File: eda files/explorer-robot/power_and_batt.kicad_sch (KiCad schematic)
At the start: 20 parts, among them J4 Conn_01x02, Q1 Q_PMOS_GSD, U7 TPS5430DDA

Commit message: Add ADR-0021 for expansion UART and camera on PIO
Add an RGB LED connector sheet to the schematic.
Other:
- title: (none) -> Battery Power input and 5V supply
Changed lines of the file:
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@@
 	(paper "A4")
 	(title_block
+		(title "Battery Power input and 5V supply")
 		(date "2026-09-27")
 		(rev "v.0.1")

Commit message: Add LiDAR power and UART interface
Add a new lidar schematic sheet with a 4-pin connector, an
AO3400A low-side MOSFET for power switching, and gate pull
resistors. Wire LIDAR_PWR, LIDAR_TX, and LIDAR_RX hierarchical
labels into the MCU sheet and update designators.

Also shorten connector value labels to BAT, LED, and MBR.
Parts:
- J4: value Conn_01x02 -> BAT
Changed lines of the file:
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@@
 			)
 		)
-		(property "Value" "Conn_01x02"
+		(property "Value" "BAT"
 			(at 177.8 64.7699 0)
 			(show_name no)

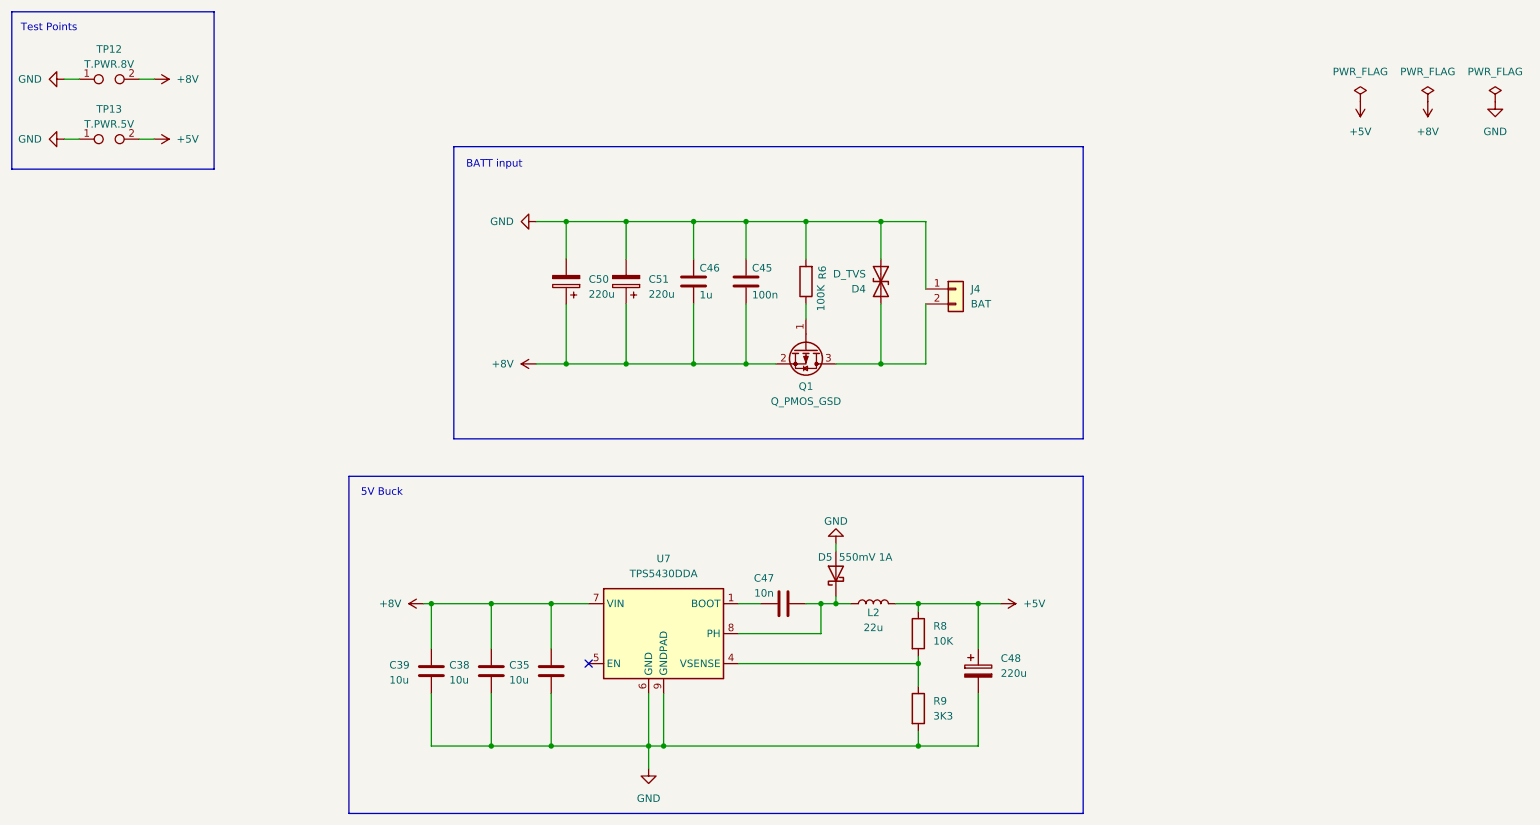
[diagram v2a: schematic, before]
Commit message: Add BATT_ADC hierarchical output to power sheet
Relocate the power/battery sheet in the schematic and expose the
battery voltage divider as a hierarchical label so it can be consumed
by the MCU.
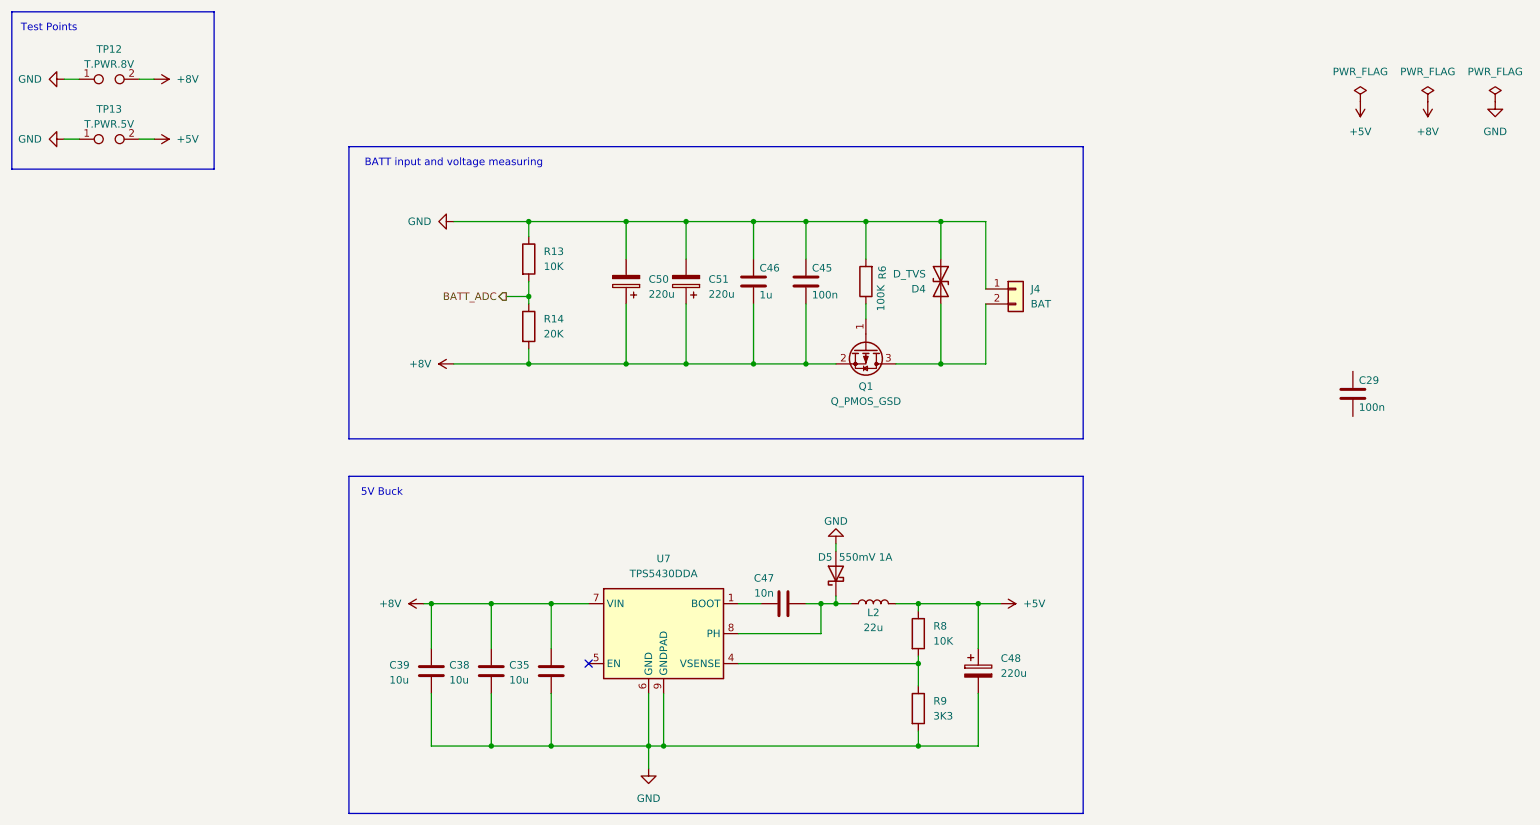
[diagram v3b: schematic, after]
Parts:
- added C29: 100n, Capacitor_SMD:C_0603_1608Metric, symbol Device:C
- added R13: 10K, Resistor_SMD:R_0603_1608Metric, symbol Device:R
- added R14: 20K, Resistor_SMD:R_0603_1608Metric, symbol Device:R
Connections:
- net +8V: now also R14.2
- net GND: now also R13.1
- new net BATT_ADC: R13.2, R14.1
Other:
- note added: "BATT input and voltage measuring"
- note removed: "BATT input"
- moved on the sheet: C45, C46, C50, C51, D4, J4, Q1, R6

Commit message: ``` Move AI camera branch to 3.3 V rail
The Grove Vision AI V2 module used here requires a 3.3 V input,
so powering it from the switched 5 V branch would over-voltage it.
Point U9 VIN at +3.3V; the TPS22917, footprint and control are
unchanged.

Also bump the 5 V inductor to 15 µH/3 A, swap the catch diode,
clean up schematic wiring and add no-connects on unused pins.
Document the decision in ADR-0025 and update ADR-0019, ADR-0021
and CONTEXT.md.
```
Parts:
- removed C29: 100n, Capacitor_SMD:C_0603_1608Metric, symbol Device:C
- D5: value 550mV 1A -> 3A 40V; JLCPCB_URL https://jlcpcb.com/partdetail/MDD_Microdiode_Semiconductor-SS14/C2480 -> https://jlcpcb.com/partdetail/MDD_Microdiode_Semiconductor-SS34/C8678; LCSC C2480 -> C8678; MPN SS14 -> SS34
- L2: value 22u -> 15u; footprint Inductor_SMD:L_APV_ANR5040 -> Inductor_SMD:L_Bourns_SRP7028A_7.3x6.6mm; JLCPCB_URL https://jlcpcb.com/partdetail/SHOUHAN-CYN504022UH/C2879700 -> https://jlcpcb.com/partdetail/SunltechTech-SLO0630H150MTT/C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; LCSC C2879700 -> C182182; MFR SHOU HAN -> Sunltech Tech; MPN CYN5040-22UH -> SLO0630H150MTT
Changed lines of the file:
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@@
 			)
 		)
-		(property "Value" "22u"
+		(property "Value" "15u"
 			(at 161.29 119.634 90)
 			(show_name no)
@@
 			)
 		)
-		(property "Footprint" "Inductor_SMD:L_APV_ANR5040"
+		(property "Footprint" "Inductor_SMD:L_Bourns_SRP7028A_7.3x6.6mm"
 			(at 161.29 115.57 0)
 			(hide yes)
@@
 			)
 		)
-		(property "JLCPCB_URL" "https://jlcpcb.com/partdetail/SHOUHAN-CYN504022UH/C2879700"
+		(property "JLCPCB_URL" "https://jlcpcb.com/partdetail/SunltechTech-SLO0630H150MTT/C182182"
 			(at 161.29 115.57 0)
 			(hide yes)
@@
 			)
 		)
-		(property "LCSC" "C2879700"
+		(property "LCSC" "C182182"
 			(at 161.29 115.57 0)
 			(hide yes)
@@
 			)
 		)
-		(property "MFR" "SHOU HAN"
+		(property "MFR" "Sunltech Tech"
 			(at 161.29 115.57 0)
 			(hide yes)
@@
 			)
 		)
-		(property "MPN" "CYN5040-22UH"
+		(property "MPN" "SLO0630H150MTT"
 			(at 161.29 115.57 0)
 			(hide yes)
@@
 			)
 		)
-		(property "Value" "550mV 1A"
+		(property "Value" "3A 40V"
 			(at 155.448 107.696 90)
 			(show_name no)
@@
 			)
 		)
-		(property "JLCPCB_URL" "https://jlcpcb.com/partdetail/MDD_Microdiode_Semiconductor-SS14/C2480"
+		(property "JLCPCB_URL" "https://jlcpcb.com/partdetail/MDD_Microdiode_Semiconductor-SS34/C8678"
 			(at 154.94 110.49 0)
 			(hide yes)
@@
 			)
 		)
-		(property "LCSC" "C2480"
+		(property "LCSC" "C8678"
 			(at 154.94 110.49 0)
 			(hide yes)
@@
 			)
 		)
-		(property "MPN" "SS14"
+		(property "MPN" "SS34"
 			(at 154.94 110.49 0)
 			(hide yes)
@@
 					(unit 1)
 				)
-			)
-		)
-	)
-	(symbol
-		(lib_id "Device:C")
-		(at 242.57 80.01 0)
-		(unit 1)
-		(body_style 1)
-		(exclude_from_sim no)
-		(in_bom yes)
-		(on_board yes)
-		(in_pos_files yes)
-		(dnp no)
-		(property "Reference" "C29"
-			(at 243.586 77.724 0)
-			(show_name no)
-			(do_not_autoplace no)
-			(effects
-				(font
-					(size 1.27 1.27)
-				)
-				(justify left)
-			)
-		)
-		(property "Value" "100n"
-			(at 243.586 82.296 0)
-			(show_name no)
-			(do_not_autoplace no)
-			(effects
-				(font
-					(size 1.27 1.27)
-				)
-				(justify left)
-			)
-		)
-		(property "Footprint" "Capacitor_SMD:C_0603_1608Metric"
-			(at 243.5352 83.82 0)
-			(hide yes)
-			(show_name no)
-			(do_not_autoplace no)
-			(effects
-				(font
-					(size 1.27 1.27)
-				)
-			)
-		)
-		(property "Datasheet" ""
-			(at 242.57 80.01 0)
-			(hide yes)
-			(show_name no)
-			(do_not_autoplace no)
-			(effects
-				(font
-					(size 1.27 1.27)
-				)
-			)
-		)
-		(property "Description" "Unpolarized capacitor"
-			(at 242.57 80.01 0)
-			(hide yes)
-			(show_name no)
-			(do_not_autoplace no)
-			(effects
-				(font
-					(size 1.27 1.27)
-				)
-			)
-		)
-		(property "MPN" "CC0603KRX7R9BB104"
-			(at 242.57 80.01 0)
-			(hide yes)
-			(show_name no)
-			(do_not_autoplace no)
-			(effects
-				(font
-					(size 1.27 1.27)
-				)
-			)
-		)
-		(property "LCSC" "C14663"
-			(at 242.57 80.01 0)
-			(hide yes)
-			(show_name no)
-			(do_not_autoplace no)
-			(effects
-				(font
-					(size 1.27 1.27)
-				)
-			)
-		)
-		(property "JLCPCB_URL" "https://jlcpcb.com/partdetail/YAGEO-CC0603KRX7R9BB104/C14663"
-			(at 242.57 80.01 0)
-			(hide yes)
-			(show_name no)
-			(do_not_autoplace no)
-			(effects
-				(font
-					(size 1.27 1.27)
-				)
-			)
-		)
-		(property "KLC_S3.3" ""
-			(at 242.57 80.01 0)
-			(hide yes)
-			(show_name no)
-			(do_not_autoplace no)
-			(effects
-				(font
-					(size 1.27 1.27)
-				)
-			)
-		)
-		(property "KLC_S4.1" ""
-			(at 242.57 80.01 0)
-			(hide yes)
-			(show_name no)
-			(do_not_autoplace no)
-			(effects
-				(font
-					(size 1.27 1.27)
-				)
-			)
-		)
-		(property "KLC_S4.2_DVDD" ""
-			(at 242.57 80.01 0)
-			(hide yes)
-			(show_name no)
-			(do_not_autoplace no)
-			(effects
-				(font
-					(size 1.27 1.27)
-				)
-			)
-		)
-		(property "KLC_S4.2_VREG_LX" ""
-			(at 242.57 80.01 0)
-			(hide yes)
-			(show_name no)
-			(do_not_autoplace no)
-			(effects
-				(font
-					(size 1.27 1.27)
-				)
-			)
-		)
-		(property "MFR" "YAGEO"
-			(at 242.57 80.01 0)
-			(hide yes)
-			(show_name no)
-			(do_not_autoplace no)
-			(effects
-				(font
-					(size 1.27 1.27)
-				)
-			)
-		)
-		(property "JLCPCP_URL" ""
-			(at 242.57 80.01 0)
-			(hide yes)
-			(show_name no)
-			(do_not_autoplace no)
-			(effects
-				(font
-					(size 1.27 1.27)
-				)
-			)
-		)
-		(pin "1"
-		)
-		(pin "2"
-		)
-		(instances
-			(project "explorer-robot"
-				(path "/57778957-dc0c-4e39-b470-8f64ada5e845/9d46820b-8f72-42a9-b57d-135ca095b278"
-					(reference "C29")
-					(unit 1)
-				)

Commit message: place test points, tidy up, ERC
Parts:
- L2: footprint Inductor_SMD:L_Bourns_SRP7028A_7.3x6.6mm -> Inductor_SMD:L_AVX_LMLP07A7
- TP12: value T.PWR.8V -> T.PWR.BAT; footprint tp:TestPoint_Bridge_Pitch3.81mm_Drill1.3mm -> Connector_PinHeader_2.54mm:PinHeader_1x02_P2.54mm_Vertical
- TP13: footprint tp:TestPoint_Bridge_Pitch3.81mm_Drill1.3mm -> Connector_PinHeader_2.54mm:PinHeader_1x02_P2.54mm_Vertical
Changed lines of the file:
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@@
 			)
 		)
-		(property "Footprint" "tp:TestPoint_Bridge_Pitch3.81mm_Drill1.3mm"
+		(property "Footprint" "Connector_PinHeader_2.54mm:PinHeader_1x02_P2.54mm_Vertical"
 			(at 31.75 36.83 0)
 			(hide yes)
@@
 			)
 		)
-		(property "Footprint" "Inductor_SMD:L_Bourns_SRP7028A_7.3x6.6mm"
+		(property "Footprint" "Inductor_SMD:L_AVX_LMLP07A7"
 			(at 161.29 115.57 0)
 			(hide yes)
@@
 			)
 		)
-		(property "Value" "T.PWR.8V"
+		(property "Value" "T.PWR.BAT"
 			(at 31.75 24.13 0)
 			(show_name no)
@@
 			)
 		)
-		(property "Footprint" "tp:TestPoint_Bridge_Pitch3.81mm_Drill1.3mm"
+		(property "Footprint" "Connector_PinHeader_2.54mm:PinHeader_1x02_P2.54mm_Vertical"
 			(at 31.75 26.67 0)
 			(hide yes)

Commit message: Update AI camera branch to 5V and document schematic
- ADR-0027 supersedes ADR-0025: AI camera input is 5V, not 3.3V
- Move U9 VIN and C55 back to +5V in aicam.kicad_sch
- Update CONTEXT.md branch descriptions and ADR cross-references
- Record ICM-20948 placement status and corrected battery divider ratio
- Adjust battery_charge_read for 33k/10k divider (0.2326 ratio)
- Enable sheet component classes; refresh netlist and PCB footprints
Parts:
- Q1: JLCPCB_URL https://jlcpcb.com/partdetail/Alpha_OmegaSemicon-AO3401A/C1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 -> https://jlcpcb.com/partdetail/Alpha_OmegaSemicon-AO3407A/C1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; LCSC C15127 -> C15155; MPN AO3401A -> AO3407A
- R14: value 20K -> 33K; JLCPCB_URL https://jlcpcb.com/partdetail/4591-0603WAF2002T5E/C4184 -> https://jlcpcb.com/partdetail/4623-0603WAF3302T5E/C4216; LCSC C4184 -> C4216; MPN 0603WAF2002T5E -> 0603WAF3302T5E
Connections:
- net BAT: now reaches D4.2 (A2), J4.2 (Pin_2), Q1.3 (D)
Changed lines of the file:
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@@
 		)
 	)
+	(label "BAT"
+		(at 180.34 73.66 0)
+		(effects
+			(font
+				(size 1.27 1.27)
+			)
+			(justify left bottom)
+		)
+	)
 	(hierarchical_label "BATT_ADC"
 		(shape output)
@@
 			)
 		)
-		(property "JLCPCB_URL" "https://jlcpcb.com/partdetail/Alpha_OmegaSemicon-AO3401A/C15127"
+		(property "JLCPCB_URL" "https://jlcpcb.com/partdetail/Alpha_OmegaSemicon-AO3407A/C15155"
 			(at 160.02 72.39 0)
 			(hide yes)
@@
 			)
 		)
-		(property "LCSC" "C15127"
+		(property "LCSC" "C15155"
 			(at 160.02 72.39 0)
 			(hide yes)
@@
 			)
 		)
-		(property "MPN" "AO3401A"
+		(property "MPN" "AO3407A"
 			(at 160.02 72.39 0)
 			(hide yes)
@@
 			)
 		)
-		(property "Value" "20K"
+		(property "Value" "33K"
 			(at 105.41 69.8499 0)
 			(show_name no)
@@
 			)
 		)
-		(property "JLCPCB_URL" "https://jlcpcb.com/partdetail/4591-0603WAF2002T5E/C4184"
+		(property "JLCPCB_URL" "https://jlcpcb.com/partdetail/4623-0603WAF3302T5E/C4216"
 			(at 102.87 68.58 0)
 			(hide yes)
@@
 			)
 		)
-		(property "LCSC" "C4184"
+		(property "LCSC" "C4216"
 			(at 102.87 68.58 0)
 			(hide yes)
@@
 			)
 		)
-		(property "MPN" "0603WAF2002T5E"
+		(property "MPN" "0603WAF3302T5E"
 			(at 102.87 68.58 0)
 			(hide yes)

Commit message: Add 1 nF CT capacitors to TPS22917 load switches
Specify C29/C30/C67/C68 on the LiDAR, AI camera, expansion and
panel branches to give a controlled rise and limit inrush. Update
ADRs 0010, 0021, 0024 and 0027 and CONTEXT.md to match, rework the
affected schematics, and swap the inductor footprint to the
EasyEDA SLO0618H part.
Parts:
- L2: footprint Inductor_SMD:L_AVX_LMLP07A7 -> easyeda imports:IND-SMD_L7.1-W6.6_SLO0618H
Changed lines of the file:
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@@
 			)
 		)
-		(property "Footprint" "Inductor_SMD:L_AVX_LMLP07A7"
+		(property "Footprint" "easyeda imports:IND-SMD_L7.1-W6.6_SLO0618H"
 			(at 161.29 115.57 0)
 			(hide yes)
